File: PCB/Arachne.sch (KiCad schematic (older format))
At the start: 0 parts

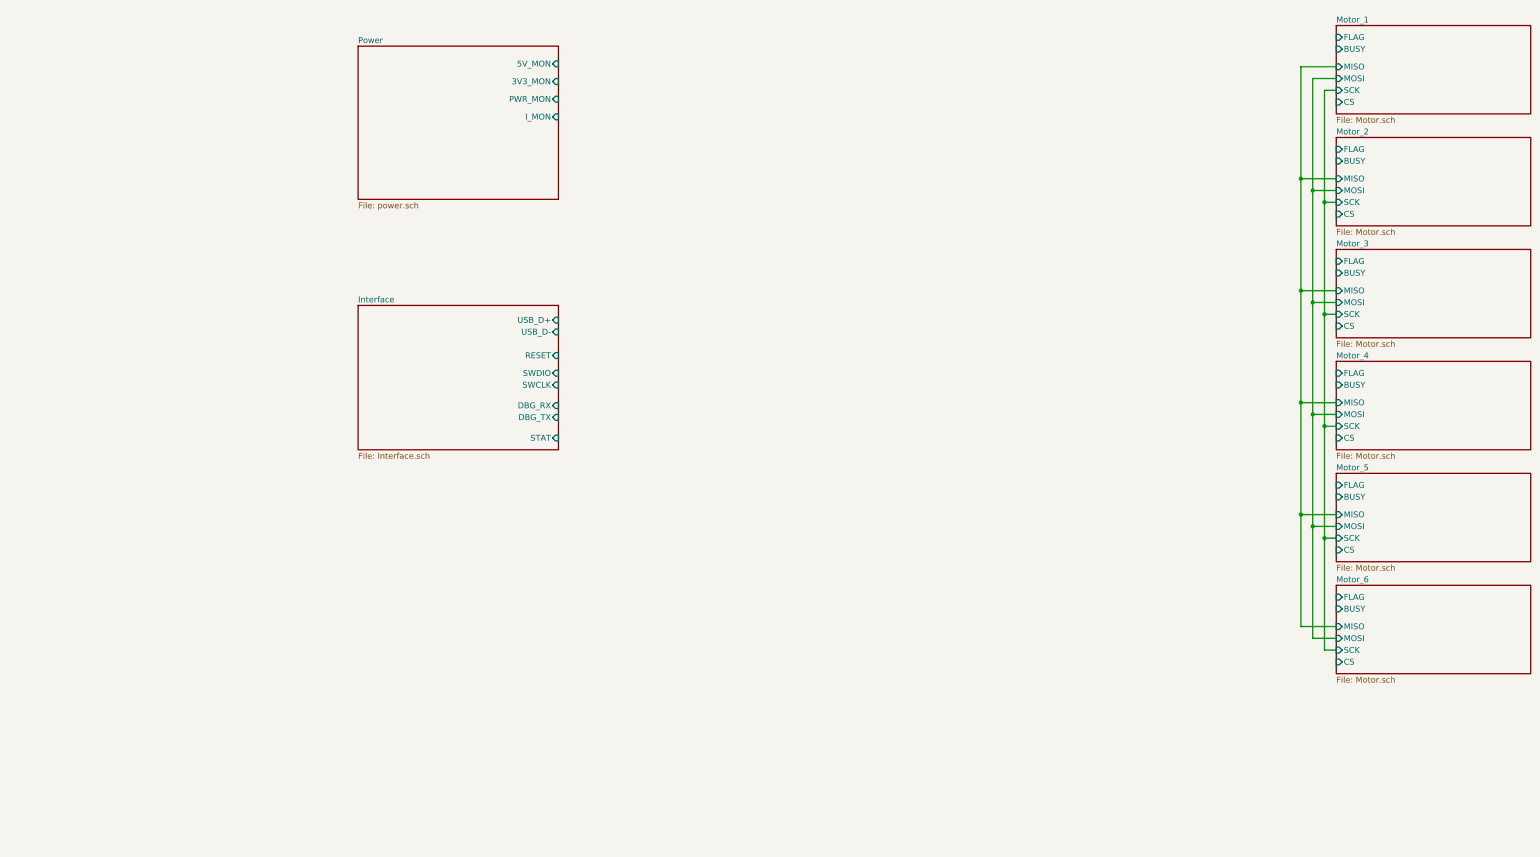
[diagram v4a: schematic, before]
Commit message: Schema: add mcu, RGB LED signalization, reset circuit
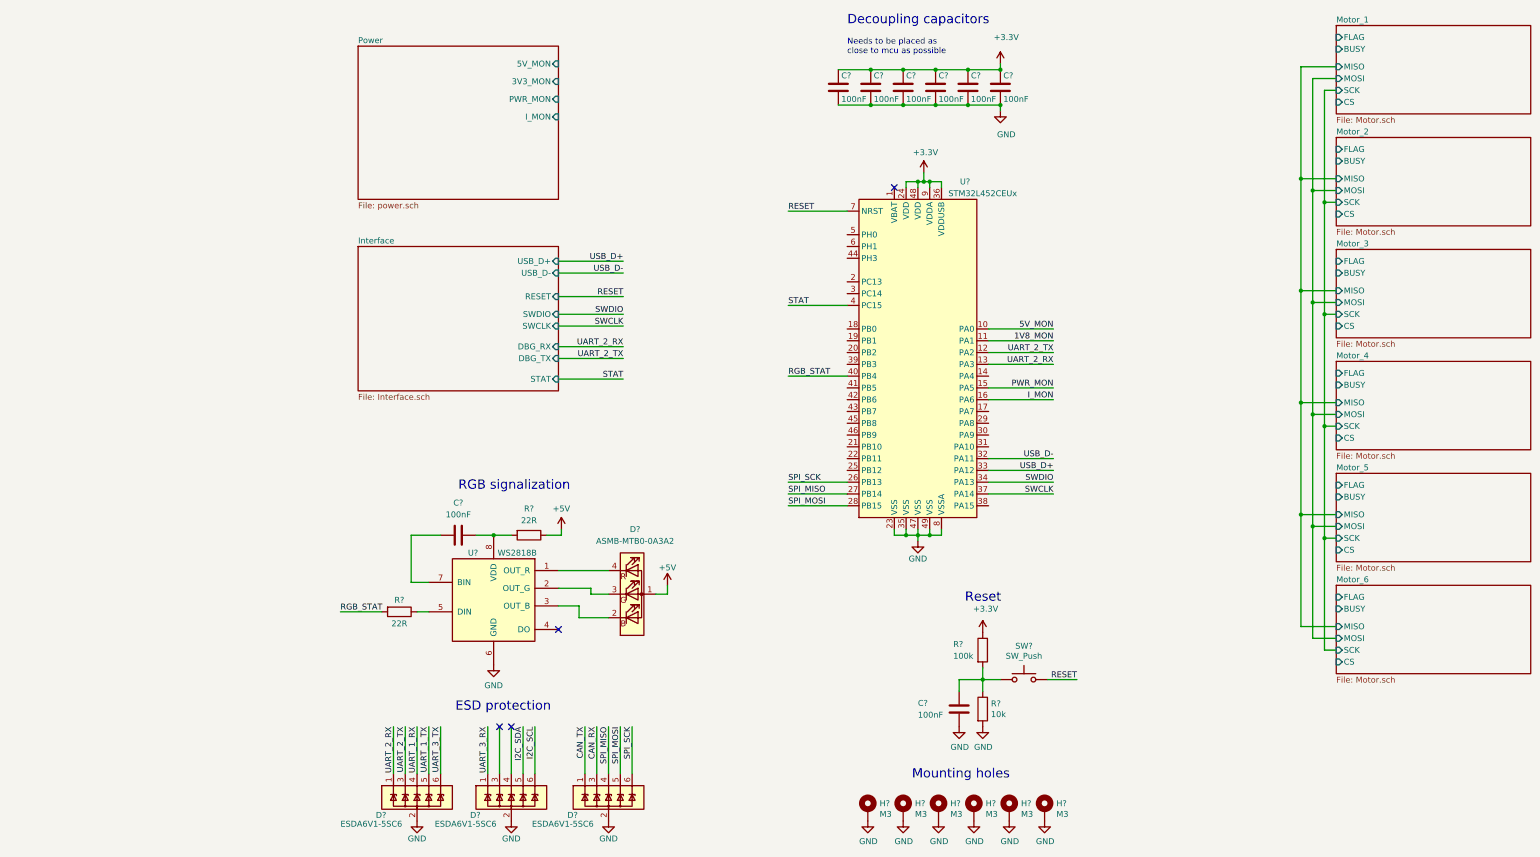
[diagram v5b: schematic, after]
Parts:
- added C? (x8): 100nF, Capacitor_SMD:C_0603_1608Metric, symbol Device:C
- added D? (x3): ESDA6V1-5SC6, Package_DFN_QFN:ST_UQFN-6L_1.5x1.7mm_Pitch0.5mm, symbol Power_Protection:ESDA6V1-5SC6
- added D?: ASMB-MTB0-0A3A2, LED_SMD:LED_Avago_PLCC4_3.2x2.8mm_CW, symbol LED:ASMB-MTB0-0A3A2
- added H? (x6): M3, MountingHole:MountingHole_3.2mm_M3_Pad_Via, symbol Mechanical:MountingHole_Pad
- added R?: 10k, Resistor_SMD:R_0603_1608Metric, symbol Device:R
- added R?: 100k, Resistor_SMD:R_0603_1608Metric, symbol Device:R
- added R? (x2): 22R, Resistor_SMD:R_0603_1608Metric, symbol Device:R
- added SW?: SW_Push, Button_Switch_SMD:SW_SPST_CK_RS282G05A3, symbol Switch:SW_Push
- added U?: STM32L452CEUx, Package_DFN_QFN:QFN-48-1EP_7x7mm_P0.5mm_EP5.15x5.15mm_ThermalVias, symbol MCU_ST_STM32L4:STM32L452CEUx
- added U?: WS2818B, Package_SO:SOP-8_3.76x4.96mm_P1.27mm, symbol TCY_IC:WS2818B
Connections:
- new net: C?.1, R?.1, R?.2, SW?.1
- new net: D?.4 (RK), U?.1 (OUT_R)
- new net: D?.3 (GK), U?.2 (OUT_G)
- new net: D?.2 (BK), U?.3 (OUT_B)
- new net: R?.1, U?.5 (DIN)
- new net: C?.2, U?.7 (BIN)
- new net: C?.1, R?.2, U?.8 (VDD)
- new net +3V3: C?.1, C?.1, C?.1, C?.1, C?.1, C?.1, R?.1, U?.24 (VDD), U?.36 (VDDUSB), U?.48 (VDD), U?.9 (VDDA)
- new net +5V: D?.1 (A), R?.1
- new net 1V8_MON: U?.11 (PA1)
- new net 5V_MON: U?.10 (PA0)
- new net CAN_RX: D?.3 (IO2)
- new net CAN_TX: D?.1 (IO1)
- new net GND: C?.2, C?.2, C?.2, C?.2, C?.2, C?.2, C?.2, D?.2 (GND), D?.2 (GND), D?.2 (GND), H?.1, H?.1, H?.1, H?.1, H?.1, H?.1, R?.2, U?.23 (VSS), U?.35 (VSS), U?.47 (VSS), U?.49 (VSS), U?.6 (GND), U?.8 (VSSA)
- new net I2C_SCL: D?.6 (IO5)
- new net I2C_SDA: D?.5 (IO4)
- new net I_MON: U?.16 (PA6)
- new net PWR_MON: U?.15 (PA5)
- new net RESET: SW?.2, U?.7 (NRST)
- new net RGB_STAT: R?.2, U?.40 (PB4)
- new net SPI_MISO: D?.4 (IO3), U?.27 (PB14)
- new net SPI_MOSI: D?.5 (IO4), U?.28 (PB15)
- new net SPI_SCK: D?.6 (IO5), U?.26 (PB13)
- new net STAT: U?.4 (PC15)
- new net SWCLK: U?.37 (PA14)
- new net SWDIO: U?.34 (PA13)
- new net UART_1_RX: D?.4 (IO3)
- new net UART_1_TX: D?.5 (IO4)
- new net UART_2_RX: D?.1 (IO1), U?.13 (PA3)
- new net UART_2_TX: D?.3 (IO2), U?.12 (PA2)
- new net UART_3_RX: D?.1 (IO1)
- new net UART_3_TX: D?.6 (IO5)
- new net USB_D+: U?.33 (PA12)
- new net USB_D-: U?.32 (PA11)
- no-connect marks 0 -> 4
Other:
- note added: "Decoupling capacitors"
- note added: "ESD protection"
- note added: "Mounting holes"
- note added: "Needs to be placed as \nclose to mcu as possible"
- note added: "RGB signalization"
- note added: "Reset"

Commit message: Schema: add FLAG and BUSY LED signalization, fix driver ground connection
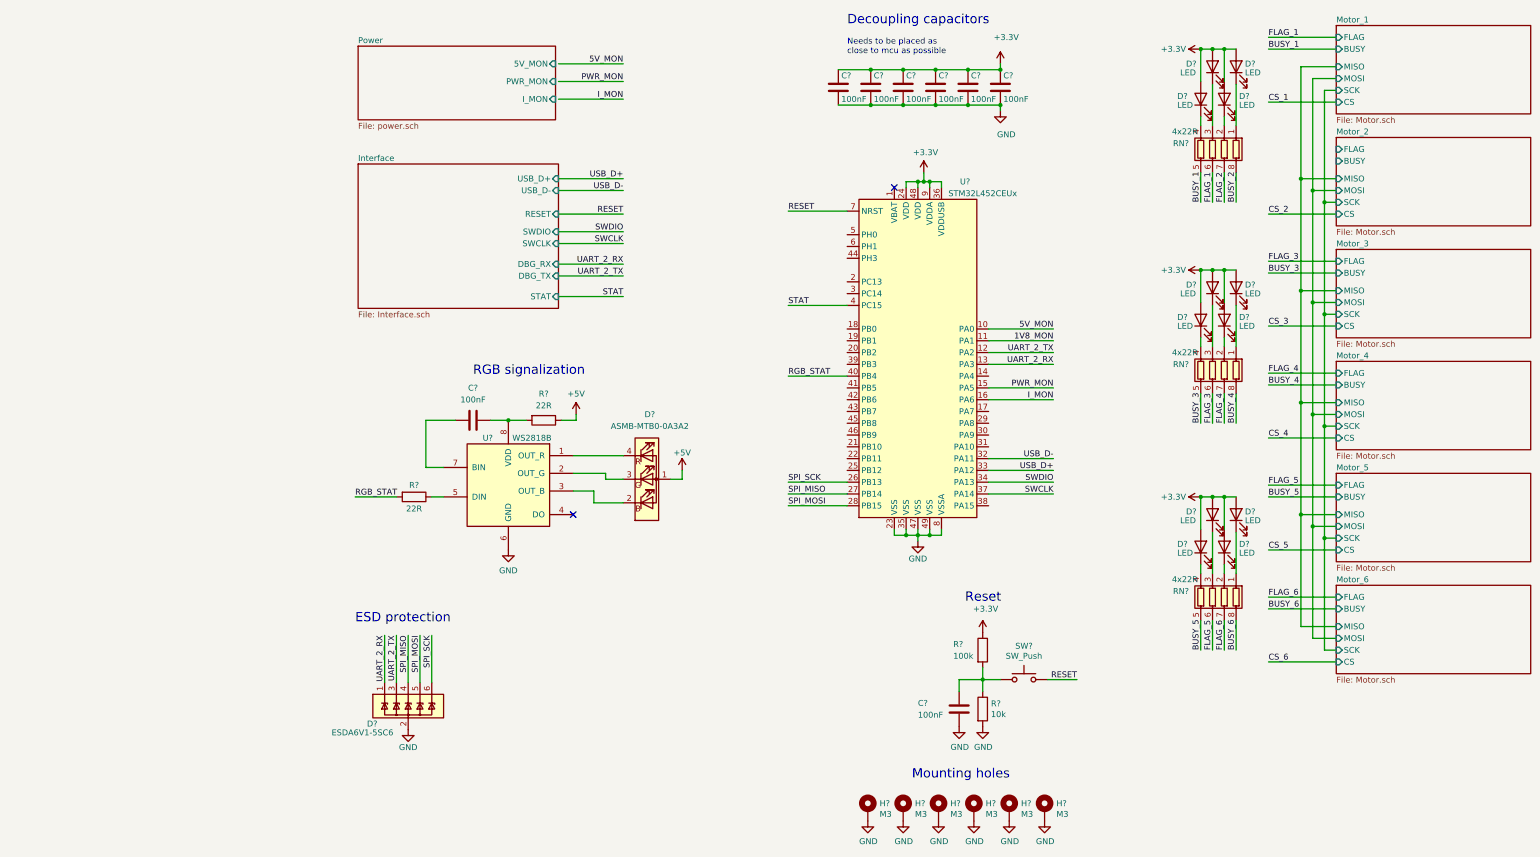
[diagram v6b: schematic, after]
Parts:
- removed D? (x2): ESDA6V1-5SC6, Package_DFN_QFN:ST_UQFN-6L_1.5x1.7mm_Pitch0.5mm, symbol Power_Protection:ESDA6V1-5SC6
- added D? (x12): LED, symbol Device:LED
- added RN? (x3): 4x22R, symbol Device:R_Pack04
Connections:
- net CAN_RX is gone; now on net UART_2_TX: D?.3 (IO2)
- net CAN_TX is gone; now on net UART_2_RX: D?.1 (IO1)
- net +3V3: now also D?.2 (A), D?.2 (A), D?.2 (A), D?.2 (A), D?.2 (A), D?.2 (A), D?.2 (A), D?.2 (A), D?.2 (A), D?.2 (A), D?.2 (A), D?.2 (A)
- new net: D?.1 (K), RN?.1 (R1.1) (x3)
- new net: D?.1 (K), RN?.2 (R2.1) (x3)
- new net: D?.1 (K), RN?.3 (R3.1) (x3)
- new net: D?.1 (K), RN?.4 (R4.1) (x3)
- new net BUSY_1: RN?.5 (R4.2)
- new net BUSY_2: RN?.8 (R1.2)
- new net BUSY_3: RN?.5 (R4.2)
- new net BUSY_4: RN?.8 (R1.2)
- new net BUSY_5: RN?.5 (R4.2)
- new net BUSY_6: RN?.8 (R1.2)
- new net FLAG_1: RN?.6 (R3.2)
- new net FLAG_2: RN?.7 (R2.2)
- new net FLAG_3: RN?.6 (R3.2)
- new net FLAG_4: RN?.7 (R2.2)
- new net FLAG_5: RN?.6 (R3.2)
- new net FLAG_6: RN?.7 (R2.2)
- no-connect marks 4 -> 2
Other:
- moved on the sheet: C?, D?, R?, U?

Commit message: Schema: new part annotation, package assignment
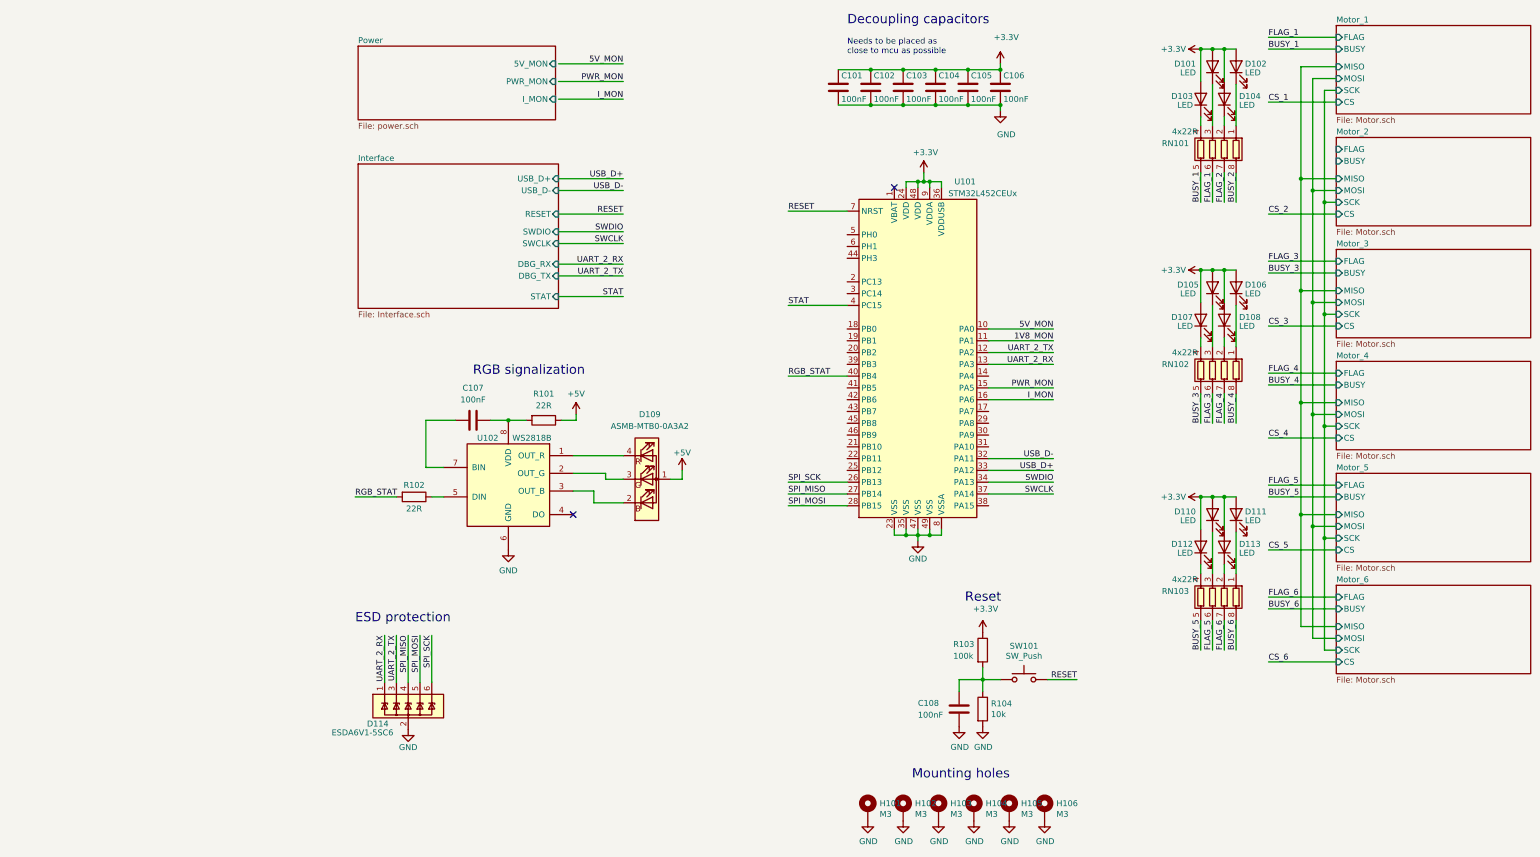
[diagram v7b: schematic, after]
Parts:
- D101, D102, D103, D104, D105, D106, D107, D108, D110, D111, D112, D113: renamed from D?; footprint (none) -> LED_SMD:LED_0603_1608Metric
- RN101, RN102, RN103: renamed from RN?; footprint (none) -> Resistor_SMD:R_Array_Convex_4x0603
- gave numbers to parts that had none: 23

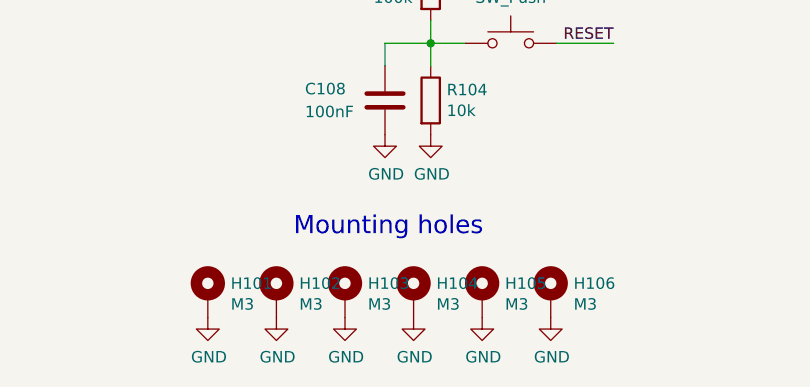
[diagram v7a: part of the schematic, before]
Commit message: PCB: routing of first part of stepper motor driver
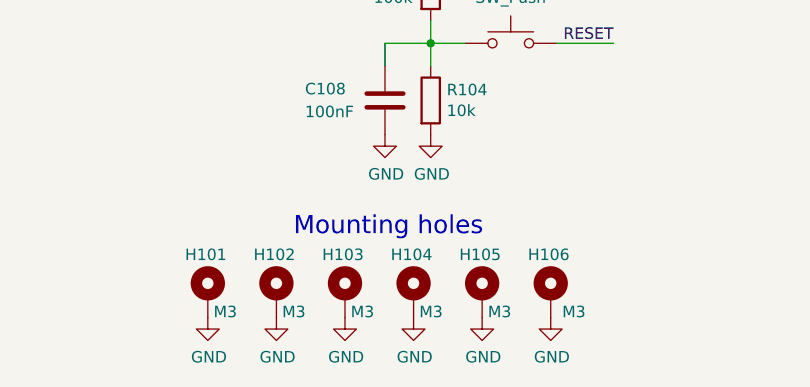
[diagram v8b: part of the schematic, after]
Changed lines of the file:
@@
 AR Path="/5E44BE52/5E45EF92" Ref="H?"  Part="1"
 AR Path="/5E45EF92" Ref="H105"  Part="1"
-F 0 "H105" H 6475 7399 50  0000 L CNN
-F 1 "M3" H 6475 7308 50  0000 L CNN
+F 0 "H105" H 6275 7525 50  0000 L CNN
+F 1 "M3" H 6400 7275 50  0000 L CNN
 F 2 "MountingHole:MountingHole_3.2mm_M3_Pad_Via" H 6375 7350 50  0001 C CNN
 F 3 "~" H 6375 7350 50  0001 C CNN
@@
 AR Path="/5E44BE52/5E45EF9E" Ref="H?"  Part="1"
 AR Path="/5E45EF9E" Ref="H104"  Part="1"
-F 0 "H104" H 6175 7399 50  0000 L CNN
-F 1 "M3" H 6175 7308 50  0000 L CNN
+F 0 "H104" H 5975 7525 50  0000 L CNN
+F 1 "M3" H 6100 7275 50  0000 L CNN
 F 2 "MountingHole:MountingHole_3.2mm_M3_Pad_Via" H 6075 7350 50  0001 C CNN
 F 3 "~" H 6075 7350 50  0001 C CNN
@@
 AR Path="/5E44BE52/5E45EFAA" Ref="H?"  Part="1"
 AR Path="/5E45EFAA" Ref="H102"  Part="1"
-F 0 "H102" H 5575 7399 50  0000 L CNN
-F 1 "M3" H 5575 7308 50  0000 L CNN
+F 0 "H102" H 5375 7525 50  0000 L CNN
+F 1 "M3" H 5500 7275 50  0000 L CNN
 F 2 "MountingHole:MountingHole_3.2mm_M3_Pad_Via" H 5475 7350 50  0001 C CNN
 F 3 "~" H 5475 7350 50  0001 C CNN
@@
 AR Path="/5E44BE52/5E45EFB0" Ref="H?"  Part="1"
 AR Path="/5E45EFB0" Ref="H103"  Part="1"
-F 0 "H103" H 5875 7399 50  0000 L CNN
-F 1 "M3" H 5875 7308 50  0000 L CNN
+F 0 "H103" H 5675 7525 50  0000 L CNN
+F 1 "M3" H 5800 7275 50  0000 L CNN
 F 2 "MountingHole:MountingHole_3.2mm_M3_Pad_Via" H 5775 7350 50  0001 C CNN
 F 3 "~" H 5775 7350 50  0001 C CNN
@@
 AR Path="/5E44BE52/5E45EFC2" Ref="H?"  Part="1"
 AR Path="/5E45EFC2" Ref="H101"  Part="1"
-F 0 "H101" H 5275 7399 50  0000 L CNN
-F 1 "M3" H 5275 7308 50  0000 L CNN
+F 0 "H101" H 5075 7525 50  0000 L CNN
+F 1 "M3" H 5200 7275 50  0000 L CNN
 F 2 "MountingHole:MountingHole_3.2mm_M3_Pad_Via" H 5175 7350 50  0001 C CNN
 F 3 "~" H 5175 7350 50  0001 C CNN
@@
 AR Path="/5E44BE52/5E45EFEA" Ref="H?"  Part="1"
 AR Path="/5E45EFEA" Ref="H106"  Part="1"
-F 0 "H106" H 6775 7399 50  0000 L CNN
-F 1 "M3" H 6775 7308 50  0000 L CNN
+F 0 "H106" H 6575 7525 50  0000 L CNN
+F 1 "M3" H 6725 7275 50  0000 L CNN
 F 2 "MountingHole:MountingHole_3.2mm_M3_Pad_Via" H 6675 7350 50  0001 C CNN
 F 3 "~" H 6675 7350 50  0001 C CNN
